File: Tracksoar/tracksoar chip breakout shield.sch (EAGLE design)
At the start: 15 parts

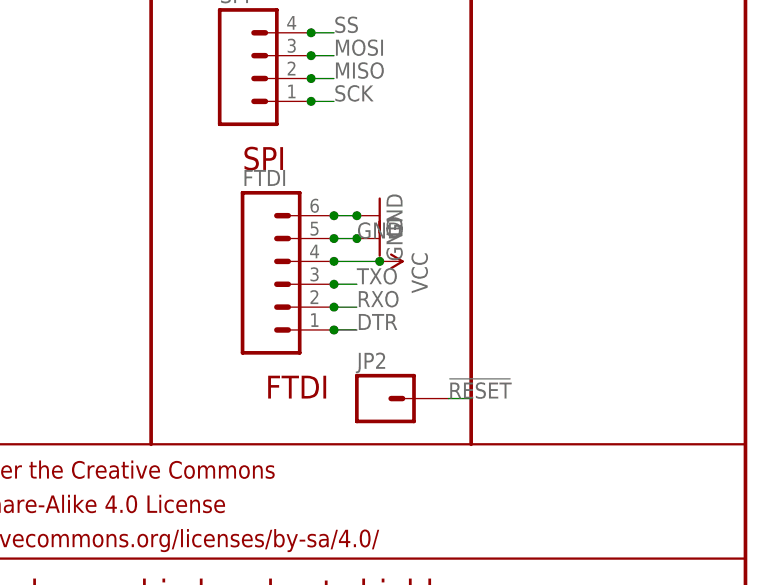
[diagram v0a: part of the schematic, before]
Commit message: replace headers
replaced 2.54mm headers on all production boards with 2mm headers to
resolve daughter board issues.
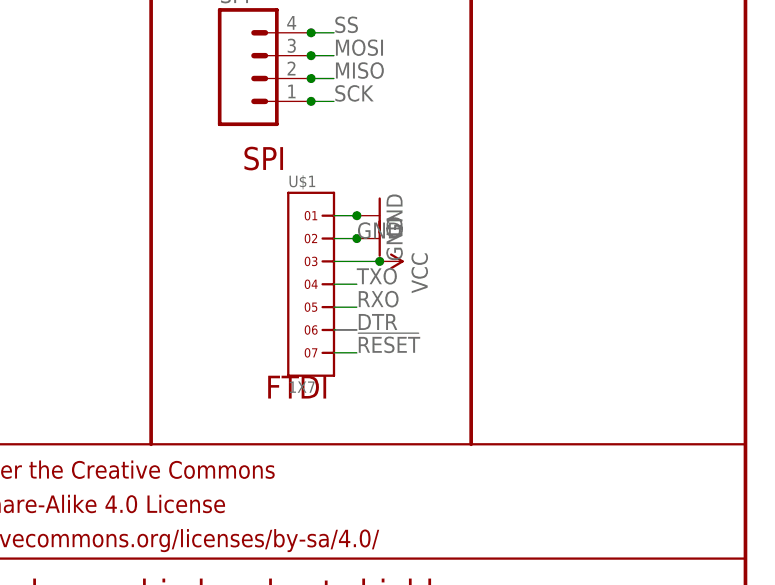
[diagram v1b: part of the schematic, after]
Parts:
- removed FTDI: (no value), SparkFun-Connectors:M06NO_SILK_FEMALE_PTH
- removed JP2: (no value), SparkFun-Connectors:M01PTH
- added U$1: 1X7, headers(2mm):1X7
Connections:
- net !RESET: now also U$1.7; no longer JP2.1
- net DTR: now also U$1.6; no longer FTDI.1
- net GND: now also U$1.1, U$1.2; no longer FTDI.5, FTDI.6
- net RXO: now also U$1.5; no longer FTDI.2
- net TXO: now also U$1.4; no longer FTDI.3
- net VCC: now also U$1.3; no longer FTDI.4
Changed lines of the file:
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@@
 </classes>
 <parts>
-<part name="FTDI" library="SparkFun-Connectors" deviceset="M06" device="NO_SILK_FEMALE_PTH"/>
 <part name="GND22" library="SparkFun-Aesthetics" deviceset="GND" device=""/>
 <part name="SUPPLY9" library="SparkFun-Aesthetics" deviceset="VCC" device=""/>
@@
 <part name="GND10" library="SparkFun-Aesthetics" deviceset="GND" device=""/>
 <part name="TX1" library="SparkFun-Connectors" deviceset="M02" device="JST-PTH-VERT" value="TX"/>
-<part name="JP2" library="SparkFun-Connectors" deviceset="M01" device="PTH"/>
 <part name="JP1" library="SparkFun-Connectors" deviceset="M05X2" device="NO_SILK"/>
 <part name="JP3" library="SparkFun-Connectors" deviceset="M05X2" device="NO_SILK"/>
@@
 <part name="SPI1" library="SparkFun-Connectors" deviceset="M04" device="JST-PTH-VERT"/>
 <part name="TX2" library="SparkFun-Connectors" deviceset="M02" device="JST-PTH-VERT" value="TX"/>
+<part name="U$1" library="headers(2mm)" deviceset="1X7" device=""/>
 </parts>
 <sheets>
@@
 </plain>
 <instances>
-<instance part="FTDI" gate="G$1" x="198.12" y="53.34"/>
 <instance part="GND22" gate="1" x="208.28" y="60.96" rot="R90"/>
 <instance part="SUPPLY9" gate="G$1" x="208.28" y="55.88" rot="R270"/>
@@
 <instance part="GND10" gate="1" x="208.28" y="58.42" rot="R90"/>
 <instance part="TX1" gate="G$1" x="193.04" y="91.44"/>
-<instance part="JP2" gate="G$1" x="208.28" y="40.64"/>
 <instance part="JP1" gate="G$1" x="30.48" y="162.56"/>
 <instance part="JP3" gate="G$1" x="50.8" y="162.56"/>
@@
 <instance part="SPI1" gate="G$1" x="147.32" y="96.52"/>
 <instance part="TX2" gate="G$1" x="144.78" y="114.3"/>
+<instance part="U$1" gate="G$1" x="200.66" y="53.34"/>
 </instances>
 <busses>
@@
 <net name="GND" class="0">
 <segment>
-<pinref part="FTDI" gate="G$1" pin="6"/>
 <wire x1="203.2" y1="60.96" x2="205.74" y2="60.96" width="0.1524" layer="91"/>
 <pinref part="GND22" gate="1" pin="GND"/>
-<junction x="203.2" y="60.96"/>
 <junction x="205.74" y="60.96"/>
-</segment>
-<segment>
-<pinref part="FTDI" gate="G$1" pin="5"/>
+<pinref part="U$1" gate="G$1" pin="1"/>
+</segment>
+<segment>
 <wire x1="203.2" y1="58.42" x2="205.74" y2="58.42" width="0.1524" layer="91"/>
 <label x="205.74" y="58.42" size="1.778" layer="95"/>
-<junction x="203.2" y="58.42"/>
 <pinref part="GND10" gate="1" pin="GND"/>
 <junction x="205.74" y="58.42"/>
+<pinref part="U$1" gate="G$1" pin="2"/>
 </segment>
 <segment>
@@
 <net name="VCC" class="0">
 <segment>
-<pinref part="FTDI" gate="G$1" pin="4"/>
 <wire x1="203.2" y1="55.88" x2="208.28" y2="55.88" width="0.1524" layer="91"/>
 <pinref part="SUPPLY9" gate="G$1" pin="VCC"/>
-<junction x="203.2" y="55.88"/>
 <junction x="208.28" y="55.88"/>
+<pinref part="U$1" gate="G$1" pin="3"/>
 </segment>
 <segment>
@@
 <net name="DTR" class="0">
 <segment>
-<pinref part="FTDI" gate="G$1" pin="1"/>
 <wire x1="203.2" y1="48.26" x2="205.74" y2="48.26" width="0.1524" layer="91"/>
 <label x="205.74" y="48.26" size="1.778" layer="95"/>
-<junction x="203.2" y="48.26"/>
+<pinref part="U$1" gate="G$1" pin="6"/>
 </segment>
 </net>
 <net name="RXO" class="0">
 <segment>
-<pinref part="FTDI" gate="G$1" pin="2"/>
 <wire x1="203.2" y1="50.8" x2="205.74" y2="50.8" width="0.1524" layer="91"/>
 <label x="205.74" y="50.8" size="1.778" layer="95"/>
-<junction x="203.2" y="50.8"/>
+<pinref part="U$1" gate="G$1" pin="5"/>
 </segment>
 </net>
 <net name="TXO" class="0">
 <segment>
-<pinref part="FTDI" gate="G$1" pin="3"/>
 <wire x1="203.2" y1="53.34" x2="205.74" y2="53.34" width="0.1524" layer="91"/>
 <label x="205.74" y="53.34" size="1.778" layer="95"/>
-<junction x="203.2" y="53.34"/>
+<pinref part="U$1" gate="G$1" pin="4"/>
 </segment>
 </net>
@@
 <net name="!RESET" class="0">
 <segment>
-<pinref part="JP2" gate="G$1" pin="1"/>
-<wire x1="215.9" y1="40.64" x2="218.44" y2="40.64" width="0.1524" layer="91"/>
-<label x="215.9" y="40.64" size="1.778" layer="95"/>
-</segment>
-</net>
+<wire x1="203.2" y1="45.72" x2="205.74" y2="45.72" width="0.1524" layer="91"/>
+<label x="205.74" y="45.72" size="1.778" layer="95"/>
+<pinref part="U$1" gate="G$1" pin="7"/>
+</segment>
+</net>
